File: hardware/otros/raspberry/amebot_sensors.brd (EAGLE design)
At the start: 80 x 29.2 mm, 17 parts

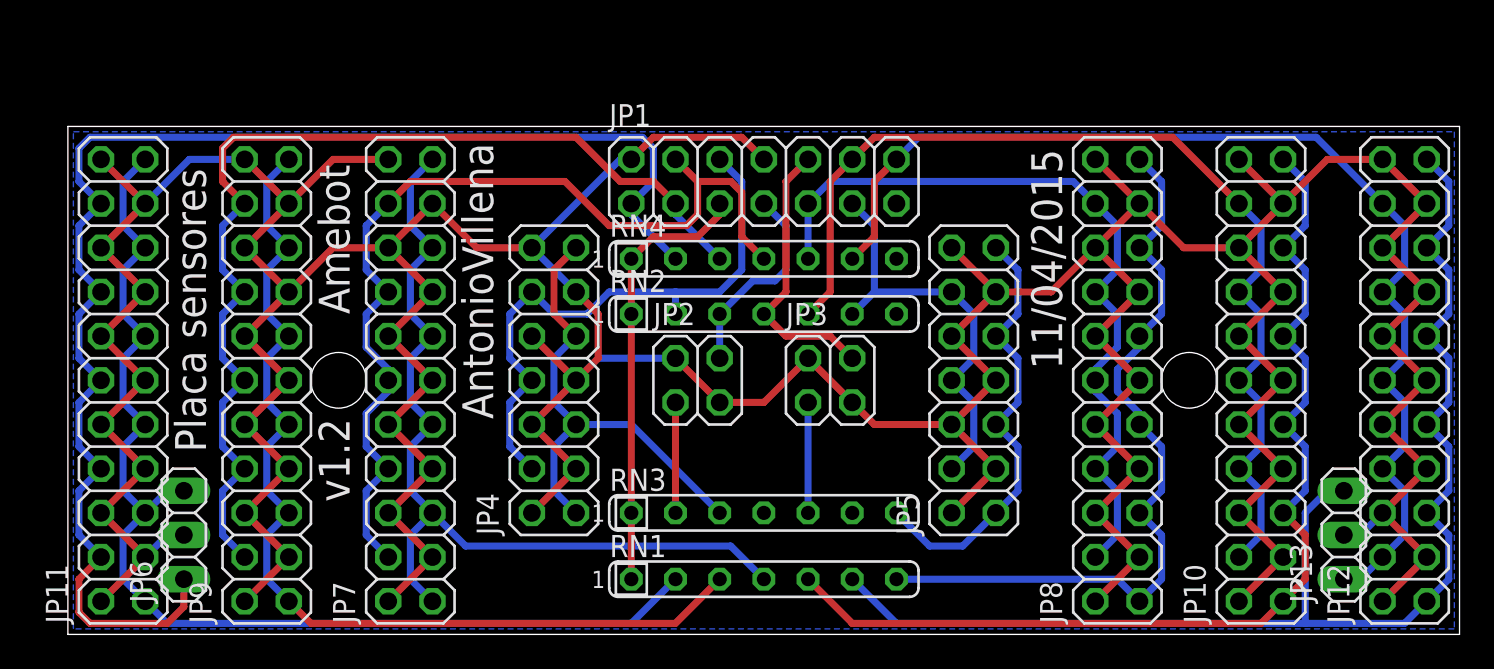
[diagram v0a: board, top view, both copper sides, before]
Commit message: cambio el común por 3.3V en lugar de masa
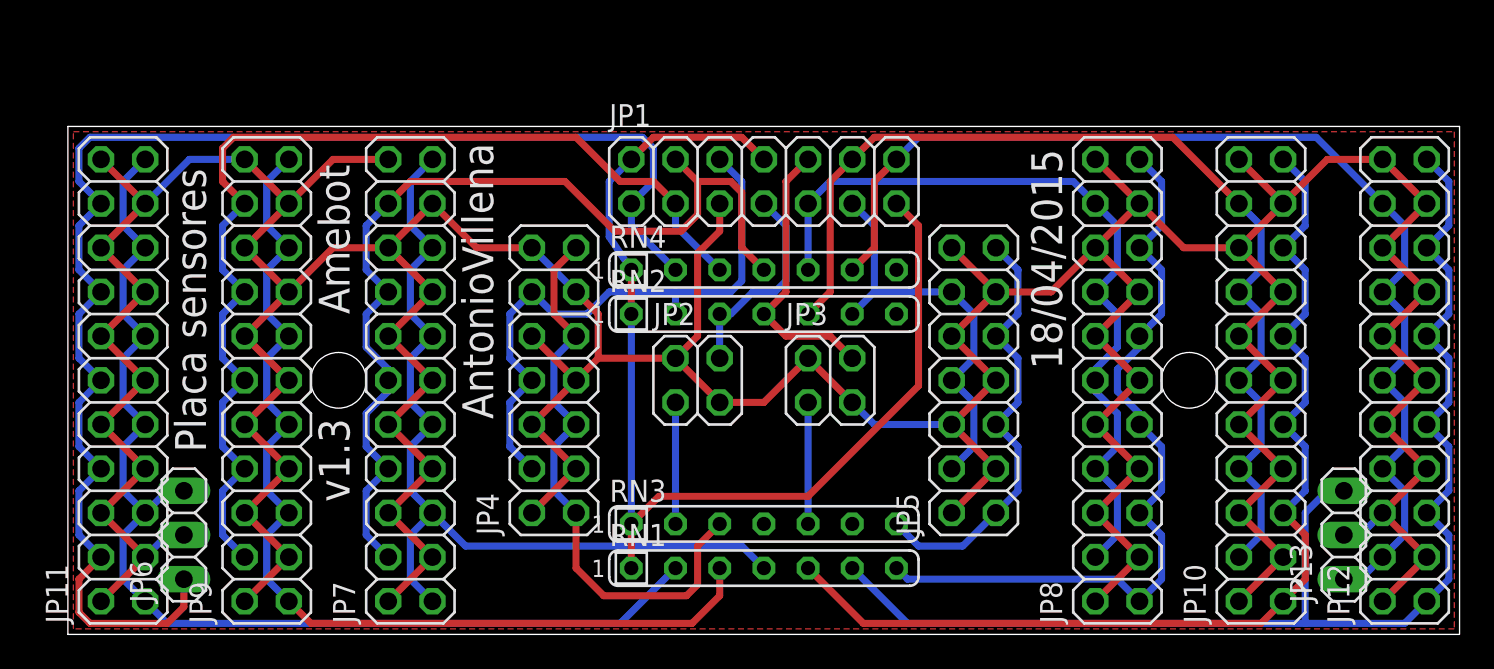
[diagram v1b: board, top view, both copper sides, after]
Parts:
- moved RN4 0.64 mm to (40.0, 21.0)
- moved RN3 0.64 mm to (40.0, 6.35)
- moved RN1 0.64 mm to (40.0, 3.81)
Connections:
- net 3.3V: now also JP10.10, JP10.11, JP10.14, JP10.15, JP10.18, JP10.19, JP10.2, JP10.22, JP10.3, JP10.6, JP10.7, JP11.10, JP11.11, JP11.14, JP11.15, JP11.18, JP11.19, JP11.2, JP11.22, JP11.3, JP11.6, JP11.7, JP12.10, JP12.11, JP12.14, JP12.15, JP12.18, JP12.19, JP12.2, JP12.22, JP12.3, JP12.6, JP12.7, JP13.2, JP2.2, JP2.3, JP3.2, JP3.3, JP4.10, JP4.11, JP4.14, JP4.2, JP4.3, JP4.6, JP4.7, JP5.10, JP5.11, JP5.14, JP5.2, JP5.3, JP5.6, JP5.7, JP6.2, JP7.10, JP7.11, JP7.14, JP7.15, JP7.18, JP7.19, JP7.2, JP7.22, JP7.3, JP7.6, JP7.7, JP8.10, JP8.11, JP8.14, JP8.15, JP8.18, JP8.19, JP8.2, JP8.22, JP8.3, JP8.6, JP8.7, JP9.10, JP9.11, JP9.14, JP9.15, JP9.18, JP9.19, JP9.2, JP9.22, JP9.3, JP9.6, JP9.7; no longer RN1.1, RN2.1, RN3.1, RN4.1
- net GND: now also RN1.1, RN2.1, RN3.1, RN4.1; no longer JP10.10, JP10.11, JP10.14, JP10.15, JP10.18, JP10.19, JP10.2, JP10.22, JP10.3, JP10.6, JP10.7, JP11.10, JP11.11, JP11.14, JP11.15, JP11.18, JP11.19, JP11.2, JP11.22, JP11.3, JP11.6, JP11.7, JP12.10, JP12.11, JP12.14, JP12.15, JP12.18, JP12.19, JP12.2, JP12.22, JP12.3, JP12.6, JP12.7, JP13.2, JP2.2, JP2.3, JP3.2, JP3.3, JP4.10, JP4.11, JP4.14, JP4.2, JP4.3, JP4.6, JP4.7, JP5.10, JP5.11, JP5.14, JP5.2, JP5.3, JP5.6, JP5.7, JP6.2, JP7.10, JP7.11, JP7.14, JP7.15, JP7.18, JP7.19, JP7.2, JP7.22, JP7.3, JP7.6, JP7.7, JP8.10, JP8.11, JP8.14, JP8.15, JP8.18, JP8.19, JP8.2, JP8.22, JP8.3, JP8.6, JP8.7, JP9.10, JP9.11, JP9.14, JP9.15, JP9.18, JP9.19, JP9.2, JP9.22, JP9.3, JP9.6, JP9.7
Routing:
- net 3.3V: track 25.2 -> 344.4 mm
- net GND: track 352.7 -> 63.9 mm
- net N$4: track 28.8 -> 33.5 mm
- net N$10: track 57.0 -> 58.2 mm
- net SEN6: track 55.0 -> 55.9 mm
- net SEN10: track 64.1 -> 64.7 mm
- net N$6: track 6.35 -> 6.99 mm
- net N$2: track 6.35 -> 6.99 mm
- net SEN2: track 60.3 -> 61.0 mm
- net SEN4: track 45.3 -> 45.9 mm
- net SEN1: track 81.7 -> 82.3 mm
- added copper zone on layer 1, net 3.3V
- removed copper zone on layer 16, net GND
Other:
- board text added: "18/04/2015"
- board text added: "v1.3"
- board text removed: "11/04/2015"
- board text removed: "v1.2"
